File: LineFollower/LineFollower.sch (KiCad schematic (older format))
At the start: 27 parts, among them Q1 Q_NPN_BCE

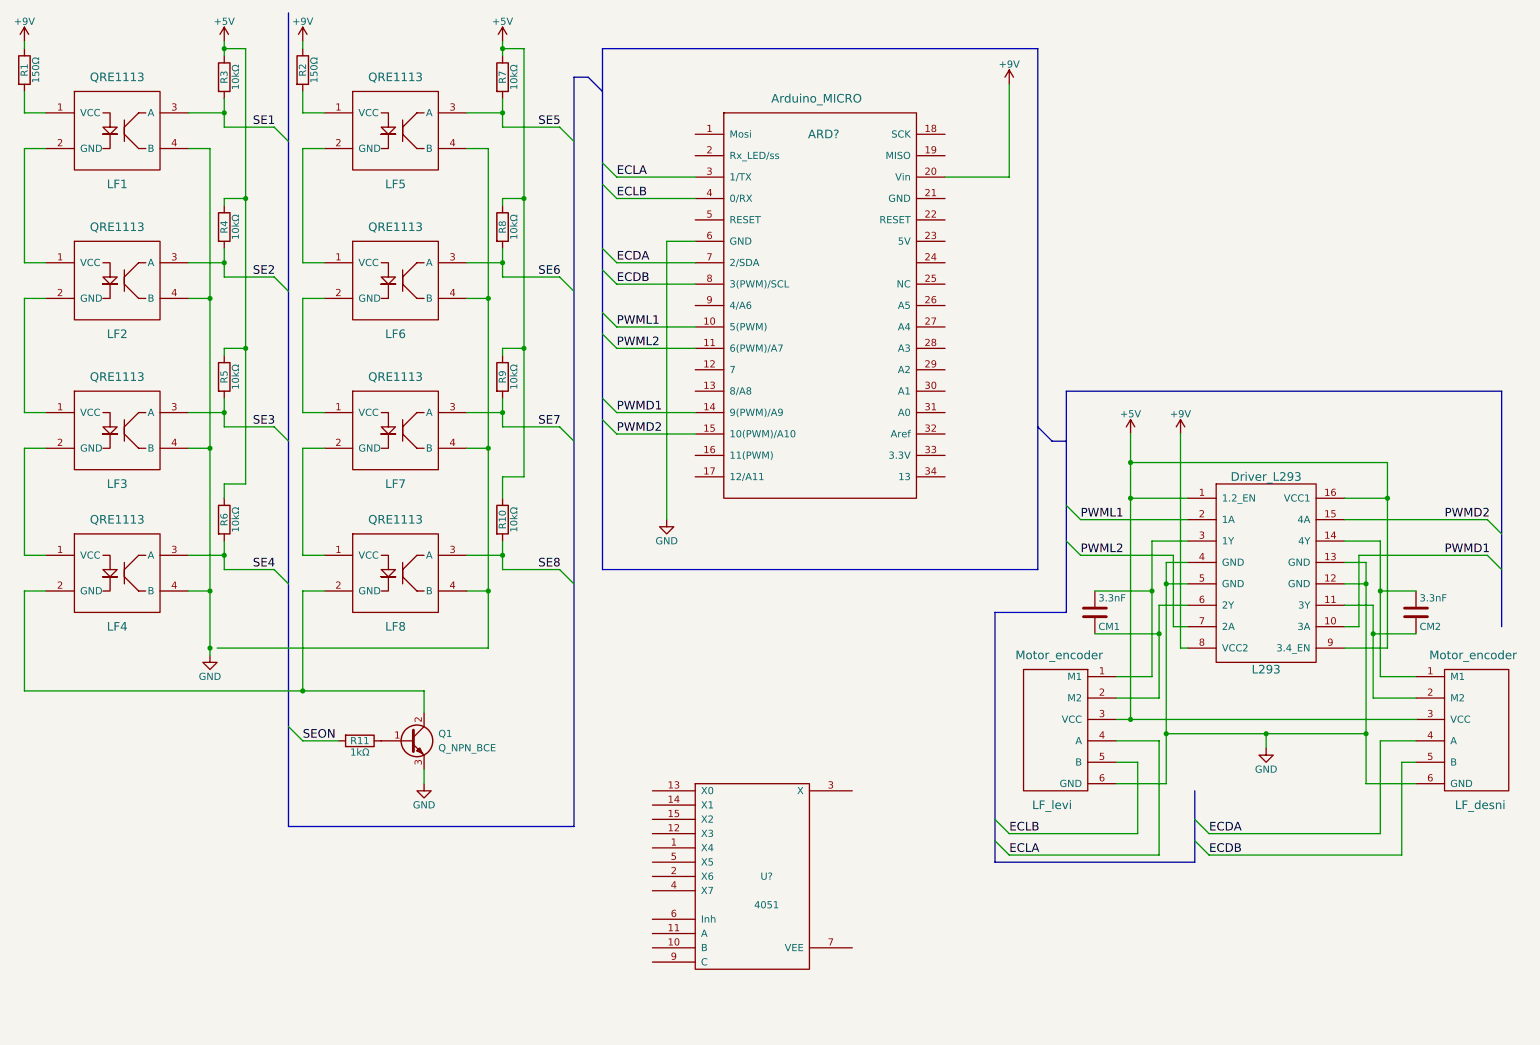
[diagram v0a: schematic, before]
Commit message: Update projektne sheme
Nekoliko dodelana projektna shema, kjer pa še vedno manjka bluetooth
modul.
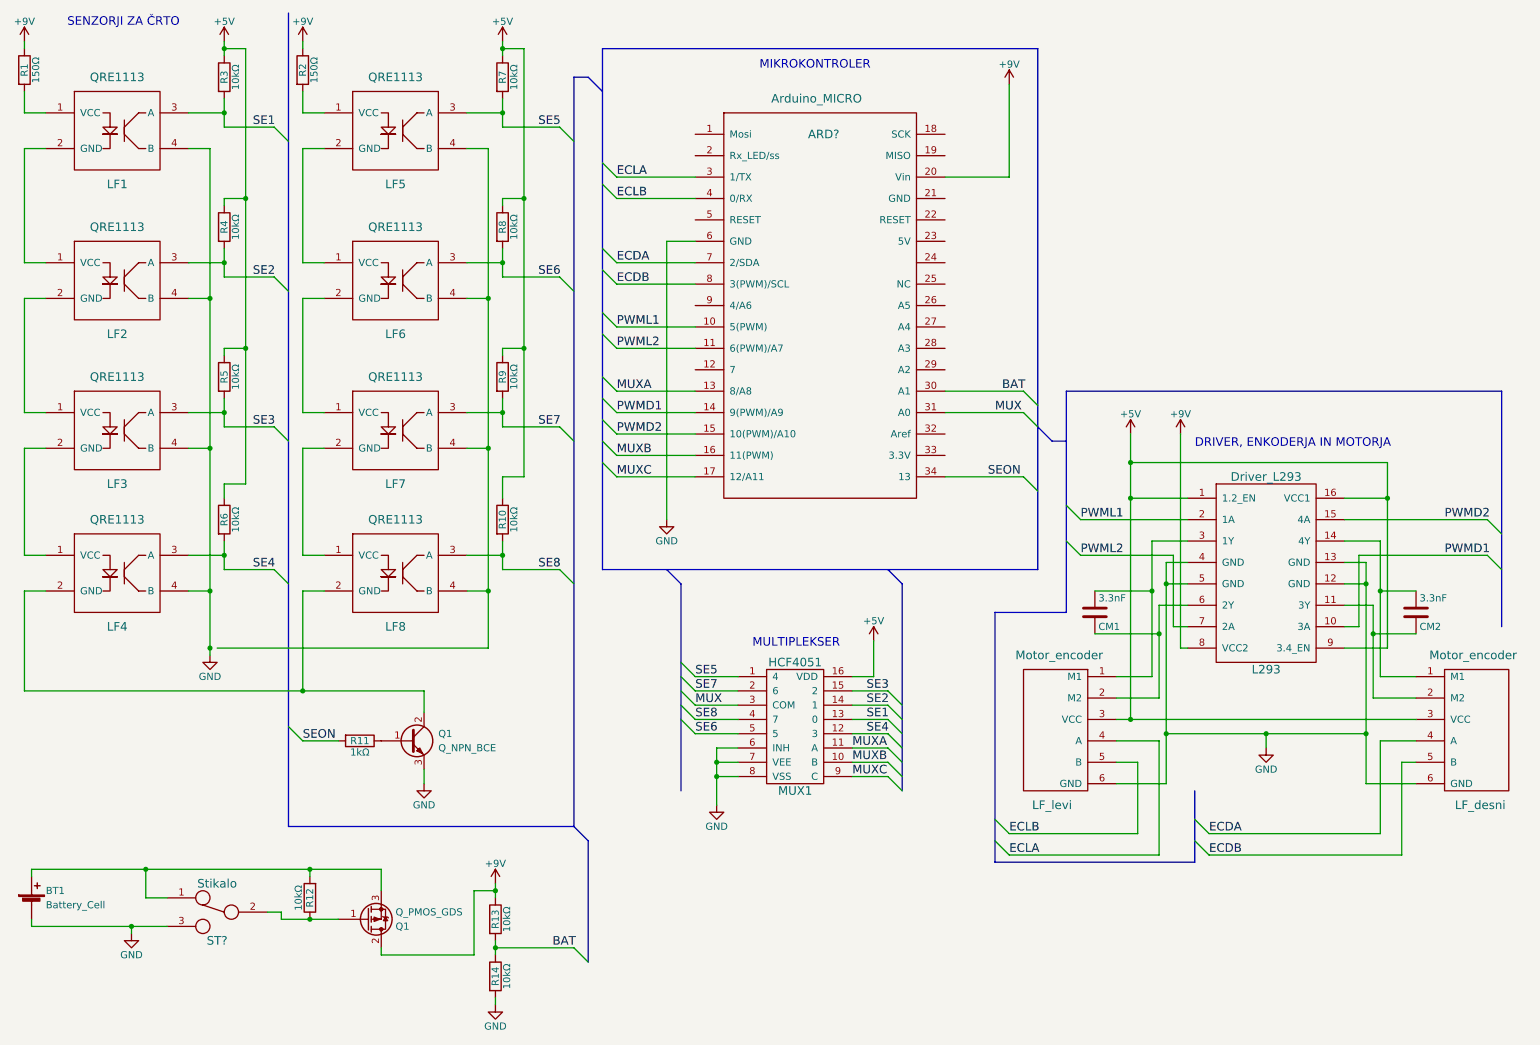
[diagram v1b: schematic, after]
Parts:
- removed U?: 4051, symbol 4051
- added 10kΩ: R12, symbol R
- added 10kΩ: R13, symbol R
- added 10kΩ: R14, symbol R
- added BT1: Battery_Cell, symbol Battery_Cell
- added MUX1: HCF4051, symbol HCF4051
- added Q1: Q_PMOS_GDS, symbol Q_PMOS_GDS
- added ST?: Stikalo, symbol Stikalo
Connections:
- net +5V: now also MUX1.16 (VDD)
- net +9V: now also 10kΩ.1, Q1.2 (D)
- net GND: now also 10kΩ.2, BT1.2 (-), MUX1.6 (INH), MUX1.7 (VEE), MUX1.8 (VSS), ST?.3
- net SE1: now also MUX1.13 (0)
- net SE2: now also MUX1.14 (1)
- net SE3: now also MUX1.15 (2)
- net SE4: now also MUX1.12 (3)
- net SE5: now also MUX1.1 (4)
- net SE6: now also MUX1.5
- net SE7: now also MUX1.2 (6)
- net SE8: now also MUX1.4 (7)
- net SEON: now also ARD?.34 (13)
- net MUXA: now reaches ARD?.13 (8/A8)
- net MUXA: now also MUX1.11 (A)
- net MUXB: now reaches ARD?.16 (11(PWM))
- net MUXB: now also MUX1.10 (B)
- net MUXC: now reaches ARD?.17 (12/A11)
- net MUXC: now also MUX1.9 (C)
- net BAT: now reaches ARD?.30 (A1)
- net BAT: now also 10kΩ.1, 10kΩ.2
- net MUX: now reaches ARD?.31 (A0)
- net MUX: now also MUX1.3 (COM)
- new net: 10kΩ.2, BT1.1 (+), Q1.3 (S), ST?.1
- new net: 10kΩ.1, Q1.1 (G), ST?.2
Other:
- note added: "DRIVER, ENKODERJA IN MOTORJA"
- note added: "MIKROKONTROLER"
- note added: "MULTIPLEKSER"
- note added: "SENZORJI ZA ČRTO"

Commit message: Dokončana projektna shema
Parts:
- added 10kΩ: R15, symbol R
- added BTM1: RN42-(Bluetooth_module), symbol RN42-(Bluetooth_module)
- added SW1: Tipka, symbol Tipka
- added VLT1: TXB0108PWR-(Voltage_level_translator), symbol TXB0108PWR-(Voltage_level_translator)
- gave numbers to parts that had none: 1
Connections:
- net +5V: now also ARD1.23 (5V), 10kΩ.1, VLT1.19 (VCCB)
- net GND: now also ARD1.21 (GND), BTM1.1 (GND), BTM1.12 (GND), BTM1.28 (GND), BTM1.29 (GND), SW1.2, VLT1.10 (OE), VLT1.11 (GND)
- net BRX: now reaches ARD1.28 (A3)
- net BRX: now also VLT1.18 (B2)
- net BTX: now reaches ARD1.29 (A2)
- net BTX: now also VLT1.20 (B1)
- net +3V3: now reaches ARD1.33 (3.3V)
- net +3V3: now also BTM1.11 (VDD), VLT1.2 (VCCA)
- net BUT: now reaches ARD1.9 (4/A6)
- net BUT: now also 10kΩ.2, SW1.1
- new net: BTM1.14 (UART_TX), VLT1.1 (A1)
- new net: BTM1.13 (UART_RX), VLT1.3 (A2)
- no-connect marks 0 -> 49
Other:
- note added: "BLUETOOTH"
- note added: "NAPAJANJE"
- note added: "TIPKA"

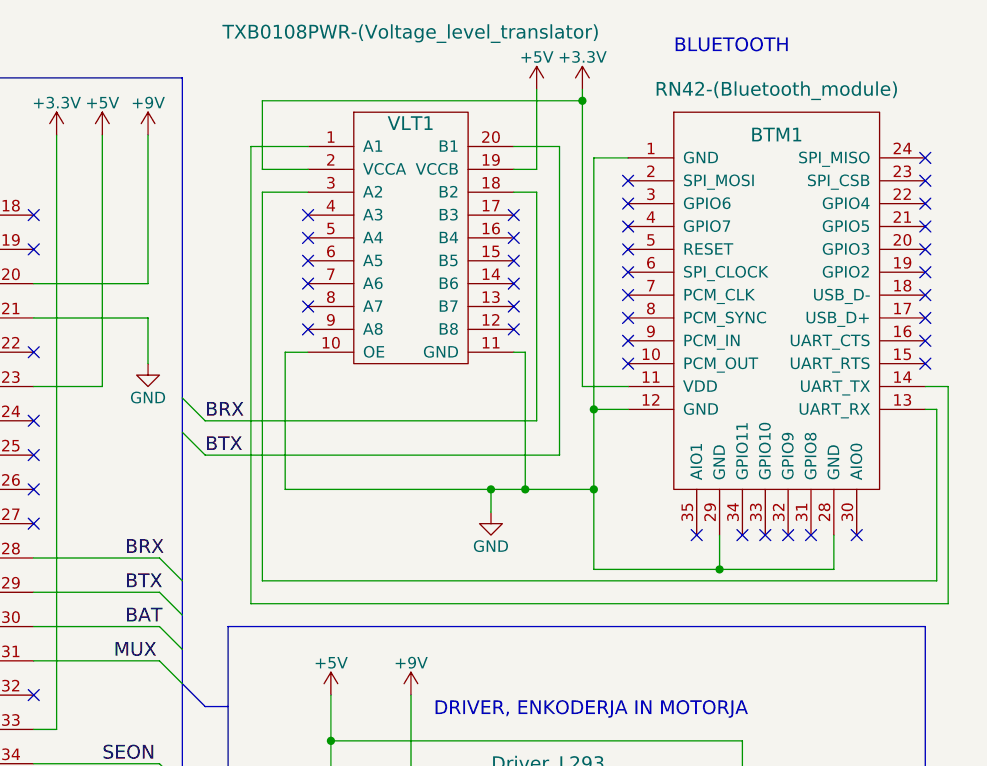
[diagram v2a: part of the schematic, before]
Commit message: Zamenjava level shifterja
Med Arduino Micro in Bluetoothe modulom je prišlo do zamenjave level
shifterja med 3v3 in 5v napetostjo, zaradi enostavnejše in cenejše
izvedbe.
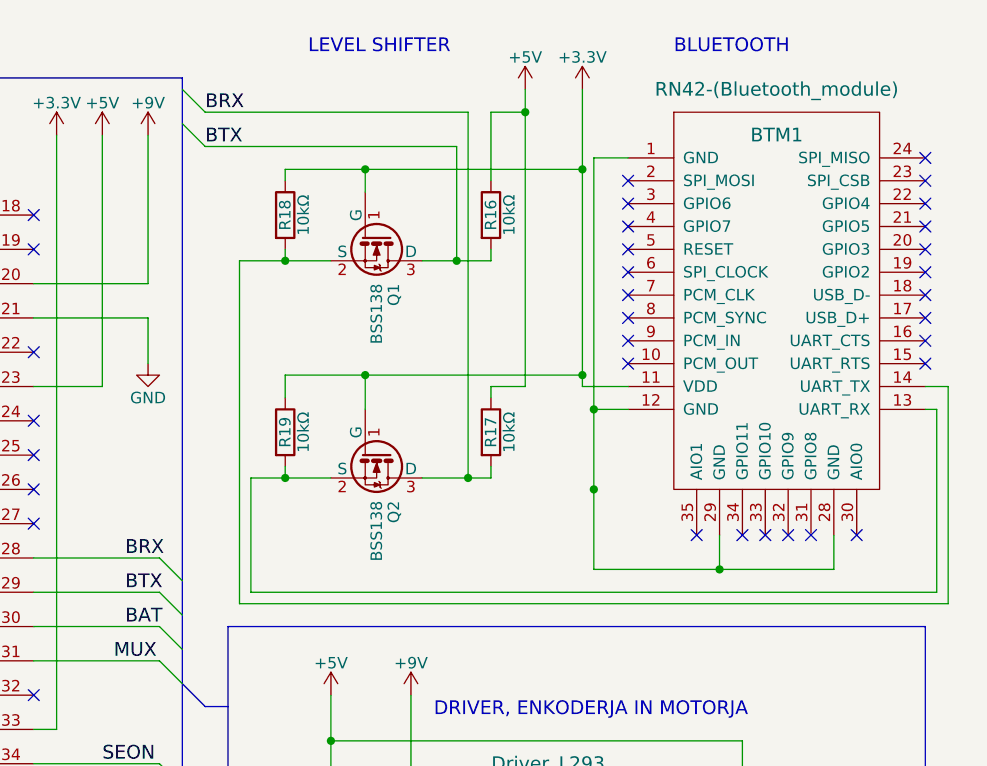
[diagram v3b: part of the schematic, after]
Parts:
- removed VLT1: TXB0108PWR-(Voltage_level_translator), symbol TXB0108PWR-(Voltage_level_translator)
- added 10kΩ: R16, symbol R
- added 10kΩ: R17, symbol R
- added 10kΩ: R18, symbol R
- added 10kΩ: R19, symbol R
- added Q1, Q2: BSS138, TO_SOT_Packages_SMD:SOT-23, symbol BSS138
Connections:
- net +3V3: now also 10kΩ.1, 10kΩ.1, Q1.1 (G), Q2.1 (G)
- net +5V: now also 10kΩ.1, 10kΩ.1
- net BRX: now also 10kΩ.2, Q2.3 (D)
- net BTX: now also 10kΩ.2, Q1.3 (D)
- net GND: no longer BTM1.1 (GND), BTM1.12 (GND), BTM1.28 (GND), BTM1.29 (GND)
- net at BTM1.14 (UART_TX): now also 10kΩ.2, Q1.2 (S)
- net at BTM1.13 (UART_RX): now also 10kΩ.2, Q2.2 (S)
- new net: BTM1.1 (GND), BTM1.12 (GND), BTM1.28 (GND), BTM1.29 (GND)
- no-connect marks 49 -> 37
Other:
- note added: "LEVEL SHIFTER"
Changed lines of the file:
@@
 BAT
-$Comp
-L TXB0108PWR-(Voltage_level_translator) VLT1
-U 1 1 58C76B2F
-P 8800 1450
-F 0 "VLT1" H 8800 1900 60  0000 C CNN
-F 1 "TXB0108PWR-(Voltage_level_translator)" H 8800 2300 60  0000 C CNN
-F 2 "" H 8850 850 60  0001 C CNN
-F 3 "http://si.farnell.com/texas-instruments/txb0108pwr/ic-translator-8bit-bidirectional/dp/1494945" H 8800 2200 60  0001 C CNN
-	1    8800 1450
-	1    0    0    -1
-$EndComp
-$Comp
-L GND #PWR?
-U 1 1 58C77F0E
-P 9150 2700
-F 0 "#PWR?" H 9150 2450 50  0001 C CNN
-F 1 "GND" H 9150 2550 50  0000 C CNN
-F 2 "" H 9150 2700 50  0000 C CNN
-F 3 "" H 9150 2700 50  0000 C CNN
-	1    9150 2700
-	1    0    0    -1
-$EndComp
 $Comp
 L +3.3V #PWR?
@@
 Text Label 7550 2900 0    60   ~ 0
 BRX
-$Comp
-L +5V #PWR?
-U 1 1 58C7BF38
-P 9350 850
-F 0 "#PWR?" H 9350 700 50  0001 C CNN
-F 1 "+5V" H 9350 990 50  0000 C CNN
-F 2 "" H 9350 850 50  0000 C CNN
-F 3 "" H 9350 850 50  0000 C CNN
-	1    9350 850
-	1    0    0    -1
-$EndComp
 Wire Wire Line
 	8350 5200 8600 5200
@@
 Wire Wire Line
 	7150 2900 7700 2900
-Wire Wire Line
-	11150 3100 8100 3100
-Wire Wire Line
-	8100 3100 8100 1100
-Wire Wire Line
-	8100 1100 8350 1100
-Wire Wire Line
-	11100 3000 8150 3000
-Wire Wire Line
-	8150 3000 8150 1300
-Wire Wire Line
-	8150 1300 8350 1300
-Wire Wire Line
-	8350 1200 8150 1200
-Wire Wire Line
-	8150 1200 8150 900
-Wire Wire Line
-	8150 900  9550 900
-Connection ~ 9550 900
-Wire Wire Line
-	9250 1200 9350 1200
-Wire Wire Line
-	9350 1200 9350 850
-Wire Wire Line
-	9250 2000 9300 2000
-Wire Wire Line
-	9250 1300 9350 1300
-Wire Wire Line
-	9350 1300 9350 2300
-Wire Wire Line
-	9350 2300 7900 2300
-Wire Wire Line
-	9250 1100 9450 1100
-Wire Wire Line
-	9450 1100 9450 2450
-Wire Wire Line
-	9450 2450 7900 2450
 Entry Wire Line
-	7800 2200 7900 2300
+	7800 850  7900 950
 Entry Wire Line
-	7800 2350 7900 2450
-Text Label 7900 2300 0    60   ~ 0
+	7800 1000 7900 1100
+Text Label 7900 950  0    60   ~ 0
 BRX
-Text Label 7900 2450 0    60   ~ 0
+Text Label 7900 1100 0    60   ~ 0
 BTX
-Wire Wire Line
-	8350 2000 8250 2000
-Wire Wire Line
-	8250 2000 8250 2600
-Wire Wire Line
-	8250 2600 9600 2600
-Connection ~ 9300 2600
-Wire Wire Line
-	9150 2700 9150 2600
-Connection ~ 9150 2600
 $Comp
 L R 10kΩ
@@
 NoConn ~ 7150 2750
 NoConn ~ 7150 3500
-NoConn ~ 8350 1400
-NoConn ~ 8350 1500
-NoConn ~ 8350 1600
-NoConn ~ 8350 1700
-NoConn ~ 8350 1800
-NoConn ~ 8350 1900
-NoConn ~ 9250 1400
-NoConn ~ 9250 1500
-NoConn ~ 9250 1600
-NoConn ~ 9250 1700
-NoConn ~ 9250 1800
-NoConn ~ 9250 1900
 Connection ~ 9600 2600
-Wire Wire Line
-	9300 2000 9300 2600
 Text Notes 2150 6450 0    60   ~ 0
 NAPAJANJE
@@
 	11150 2150 11050 2150
 Wire Wire Line
-	11100 3000 11100 2250
+	11100 2250 11100 3050
 Wire Wire Line
 	11100 2250 11050 2250
@@
 Text Notes 9950 700  0    60   ~ 0
 BLUETOOTH
+$Comp
+L BSS138 Q1
+U 1 1 58CE6610
+P 8650 1500
+F 0 "Q1" H 8850 1575 50  0000 L CNN
+F 1 "BSS138" H 8850 1500 50  0000 L CNN
+F 2 "TO_SOT_Packages_SMD:SOT-23" H 8850 1425 50  0001 L CIN
+F 3 "" H 8650 1500 50  0000 L CNN
+	1    8650 1500
+	0    1    1    0
+$EndComp
+$Comp
+L BSS138 Q2
+U 1 1 58CE6CBE
+P 8650 2450
+F 0 "Q2" H 8850 2525 50  0000 L CNN
+F 1 "BSS138" H 8850 2450 50  0000 L CNN
+F 2 "TO_SOT_Packages_SMD:SOT-23" H 8850 2375 50  0001 L CIN
+F 3 "" H 8650 2450 50  0000 L CNN
+	1    8650 2450
+	0    1    1    0
+$EndComp
+Wire Wire Line
+	7900 950  9050 950
+Wire Wire Line
+	8250 2100 9550 2100
+Connection ~ 9550 2100
+Wire Wire Line
+	8600 1300 8600 1200
+Wire Wire Line
+	8250 1200 9550 1200
+Connection ~ 9550 1200
+Wire Wire Line
+	7900 1100 9000 1100
+Wire Wire Line
+	9000 1100 9000 1600
+Wire Wire Line
+	8450 1600 8050 1600
+Wire Wire Line
+	8050 1600 8050 3100
+Wire Wire Line
+	8050 3100 11150 3100
+Wire Wire Line
+	11100 3050 8100 3050
+Wire Wire Line
+	8100 3050 8100 2550
+Wire Wire Line
+	8100 2550 8450 2550
+Wire Wire Line
+	8600 2250 8600 2100
+Wire Wire Line
+	8850 2550 9150 2550
+Wire Wire Line
+	9050 950  9050 2550
+$Comp
+L R 10kΩ
+U 1 1 58CF09EC
+P 9150 1400
+F 0 "10kΩ" V 9230 1400 50  0000 C CNN
+F 1 "R16" V 9150 1400 50  0000 C CNN
+F 2 "" V 9080 1400 50  0000 C CNN
+F 3 "" H 9150 1400 50  0000 C CNN
+	1    9150 1400
+	1    0    0    -1
+$EndComp
+$Comp
+L R 10kΩ
+U 1 1 58CF0A7B
+P 9150 2350
+F 0 "10kΩ" V 9230 2350 50  0000 C CNN
+F 1 "R17" V 9150 2350 50  0000 C CNN
+F 2 "" V 9080 2350 50  0000 C CNN
+F 3 "" H 9150 2350 50  0000 C CNN
+	1    9150 2350
+	1    0    0    -1
+$EndComp
+Connection ~ 9000 1600
+$Comp
+L +5V #PWR?
+U 1 1 58C7BF38
+P 9300 850
+F 0 "#PWR?" H 9300 700 50  0001 C CNN
+F 1 "+5V" H 9300 990 50  0000 C CNN
+F 2 "" H 9300 850 50  0000 C CNN
+F 3 "" H 9300 850 50  0000 C CNN
+	1    9300 850
+	1    0    0    -1
+$EndComp
+Wire Wire Line
+	8850 1600 9150 1600
+Wire Wire Line
+	9150 1600 9150 1550
+Wire Wire Line
+	9150 1250 9150 950
+Wire Wire Line
+	9150 950  9300 950
+Wire Wire Line
+	9300 850  9300 2150
+Wire Wire Line
+	9300 2150 9150 2150
+Wire Wire Line
+	9150 2150 9150 2200
+Connection ~ 9300 950
+Wire Wire Line
+	9150 2550 9150 2500
+Connection ~ 9050 2550
+$Comp
+L R 10kΩ
+U 1 1 58CF6830
+P 8250 1400
+F 0 "10kΩ" V 8330 1400 50  0000 C CNN
+F 1 "R18" V 8250 1400 50  0000 C CNN
+F 2 "" V 8180 1400 50  0000 C CNN
+F 3 "" H 8250 1400 50  0000 C CNN
+	1    8250 1400
+	1    0    0    -1
+$EndComp
+$Comp
+L R 10kΩ
+U 1 1 58CF68D1
+P 8250 2350
+F 0 "10kΩ" V 8330 2350 50  0000 C CNN
+F 1 "R19" V 8250 2350 50  0000 C CNN
+F 2 "" V 8180 2350 50  0000 C CNN
+F 3 "" H 8250 2350 50  0000 C CNN
+	1    8250 2350
+	1    0    0    -1
+$EndComp
+Wire Wire Line
+	8250 1200 8250 1250
+Connection ~ 8600 1200
+Wire Wire Line
+	8250 1550 8250 1600
+Connection ~ 8250 1600
+Wire Wire Line
+	8250 2100 8250 2200
+Connection ~ 8600 2100
+Wire Wire Line
+	8250 2500 8250 2550
+Connection ~ 8250 2550
+Text Notes 8350 700  0    60   ~ 0
+LEVEL SHIFTER
 $EndSCHEMATC
